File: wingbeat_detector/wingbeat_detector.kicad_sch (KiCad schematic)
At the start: 0 parts

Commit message: Rename to wingbeat_detector
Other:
- title: light_sensor_opt101 -> wingbeat_detector
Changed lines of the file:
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@@
   (paper "A4")
   (title_block
-    (title "light_sensor_opt101")
+    (title "wingbeat_detector")
     (date "2022-11-18")
     (rev "3.0.0")

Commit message: Add symbols and documentation
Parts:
- added P1: CONN_02X04_IC_DIP_RA_VERT, Janelia:HEADER_02x04, symbol Janelia:CONN_02X04_IC_DIP_RA_VERT
- added U1: UAF42, Janelia:SOIC_16, symbol Janelia:UAF42
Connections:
- no-connect marks 0 -> 2
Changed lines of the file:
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@@
   (title_block
     (title "wingbeat_detector")
-    (date "2022-11-18")
+    (date "2023-02-23")
     (rev "3.0.0")
     (company "Howard Hughes Medical Institute")
   )
+  (no_connect (at 96.52 81.28))
+  (no_connect (at 96.52 83.82))
+  (symbol (lib_id "Janelia:CONN_02X04_IC_DIP_RA_VERT") (at 90.17 82.55 0) (unit 1)
+    (in_bom yes) (on_board yes) (dnp no)
+    (property "Reference" "P1" (at 90.17 76.2 0)
+      (effects (font (size 1.27 1.27)))
+    )
+    (property "Value" "CONN_02X04_IC_DIP_RA_VERT" (at 90.17 88.9 0)
+      (effects (font (size 1.27 1.27)))
+    )
+    (property "Footprint" "Janelia:HEADER_02x04" (at 90.17 113.03 0)
+      (effects (font (size 1.524 1.524)) hide)
+    )
+    (property "Datasheet" "" (at 90.17 113.03 0)
+      (effects (font (size 1.524 1.524)))
+    )
+    (property "Vendor" "Digi-Key" (at 92.71 73.66 0)
+      (effects (font (size 1.524 1.524)) hide)
+    )
+    (property "Vendor Part Number" "A117-ND" (at 95.25 71.12 0)
+      (effects (font (size 1.524 1.524)) hide)
+    )
+    (property "Description" "CONN IC DIP SOCKET 8POS GOLD" (at 97.79 68.58 0)
+      (effects (font (size 1.524 1.524)) hide)
+    )
+    (property "Manufacturer" "Aries Electronics" (at 90.17 96.52 0)
+      (effects (font (size 1.27 1.27)) hide)
+    )
+    (property "Manufacturer Part Number" "08-810-90" (at 90.17 93.98 0)
+      (effects (font (size 1.27 1.27)) hide)
+    )
+    (pin "1")
+    (pin "2")
+    (pin "3")
+    (pin "4")
+    (pin "5")
+    (pin "6")
+    (pin "7")
+    (pin "8")
+    (instances
+      (project "wingbeat_detector"
+        (path "/cc457ebc-4af6-4663-b19f-8cb38f061cb4"
+          (reference "P1") (unit 1)
+        )
+      )
+    )
+  )
+  (symbol (lib_id "Janelia:UAF42") (at 162.56 83.82 0) (unit 1)
+    (in_bom yes) (on_board yes) (dnp no) (fields_autoplaced)
+    (property "Reference" "U1" (at 193.04 72.2883 0)
+      (effects (font (size 1.524 1.524)))
+    )
+    (property "Value" "UAF42" (at 193.04 74.8283 0)
+      (effects (font (size 1.524 1.524)))
+    )
+    (property "Footprint" "Janelia:SOIC_16" (at 184.15 72.39 0)
+      (effects (font (size 1.524 1.524)) hide)
+    )
+    (property "Datasheet" "" (at 186.69 69.85 0)
+      (effects (font (size 1.524 1.524)))
+    )
+    (property "Vendor" "Digi-Key" (at 189.23 67.31 0)
+      (effects (font (size 1.524 1.524)) hide)
+    )
+    (property "Vendor Part Number" "UAF42AU-ND" (at 191.77 64.77 0)
+      (effects (font (size 1.524 1.524)) hide)
+    )
+    (property "Description" "IC UNIV ACTIVE FILTER 16-SOIC" (at 194.31 62.23 0)
+      (effects (font (size 1.524 1.524)) hide)
+    )
+    (property "Manufacturer" "Texas Instruments" (at 162.56 83.82 0)
+      (effects (font (size 1.27 1.27)) hide)
+    )
+    (property "Manufacturer Part Number" "UAF42AU" (at 162.56 83.82 0)
+      (effects (font (size 1.27 1.27)) hide)
+    )
+    (pin "1")
+    (pin "10")
+    (pin "11")
+    (pin "12")
+    (pin "13")
+    (pin "14")
+    (pin "15")
+    (pin "16")
+    (pin "2")
+    (pin "3")
+    (pin "4")
+    (pin "5")
+    (pin "6")
+    (pin "7")
+    (pin "8")
+    (pin "9")
+    (instances
+      (project "wingbeat_detector"
+        (path "/cc457ebc-4af6-4663-b19f-8cb38f061cb4"
+          (reference "U1") (unit 1)
+        )
+      )
+    )
+  )
   (sheet_instances

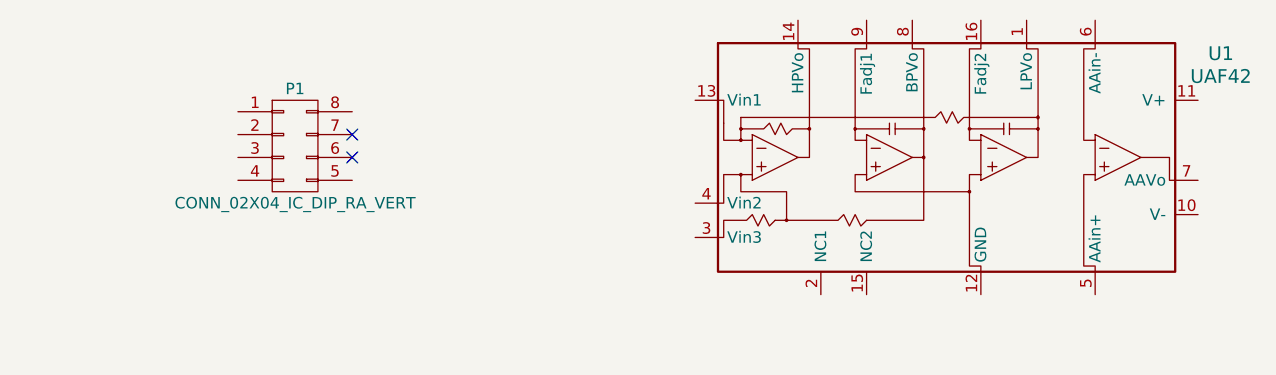
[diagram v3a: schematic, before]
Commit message: Add documentation and initial schematic part
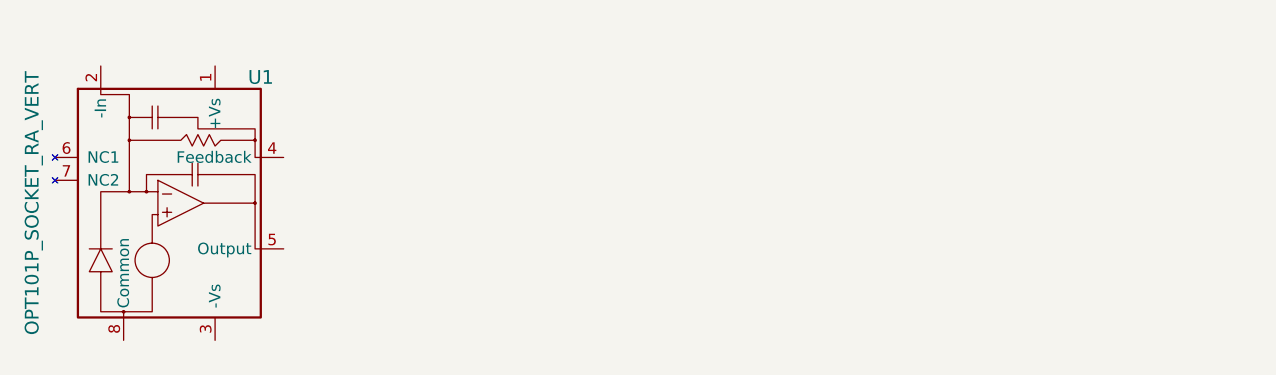
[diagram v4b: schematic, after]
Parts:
- removed P1: CONN_02X04_IC_DIP_RA_VERT, Janelia:HEADER_02x04, symbol Janelia:CONN_02X04_IC_DIP_RA_VERT
- removed U1: UAF42, Janelia:SOIC_16, symbol Janelia:UAF42
- added U1: OPT101P_SOCKET_RA_VERT, Janelia:SOCKET_DIP_02x04_RA_VERT, symbol Janelia:OPT101P_SOCKET_RA_VERT
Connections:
- no-connect marks 2 -> 0
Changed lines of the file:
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@@
     (company "Howard Hughes Medical Institute")
   )
-  (no_connect (at 96.52 81.28))
-  (no_connect (at 96.52 83.82))
-  (symbol (lib_id "Janelia:CONN_02X04_IC_DIP_RA_VERT") (at 90.17 82.55 0) (unit 1)
+  (symbol (lib_id "Janelia:OPT101P_SOCKET_RA_VERT") (at 76.2 88.9 0) (unit 1)
     (in_bom yes) (on_board yes) (dnp no)
-    (property "Reference" "P1" (at 90.17 76.2 0)
-      (effects (font (size 1.27 1.27)))
-    )
-    (property "Value" "CONN_02X04_IC_DIP_RA_VERT" (at 90.17 88.9 0)
-      (effects (font (size 1.27 1.27)))
-    )
-    (property "Footprint" "Janelia:HEADER_02x04" (at 90.17 113.03 0)
-      (effects (font (size 1.524 1.524)) hide)
-    )
-    (property "Datasheet" "" (at 90.17 113.03 0)
+    (property "Reference" "U1" (at 86.36 74.93 0)
       (effects (font (size 1.524 1.524)))
     )
-    (property "Vendor" "Digi-Key" (at 92.71 73.66 0)
-      (effects (font (size 1.524 1.524)) hide)
+    (property "Value" "OPT101P_SOCKET_RA_VERT" (at 60.96 88.9 90)
+      (effects (font (size 1.524 1.524)))
     )
-    (property "Vendor Part Number" "A117-ND" (at 95.25 71.12 0)
-      (effects (font (size 1.524 1.524)) hide)
-    )
-    (property "Description" "CONN IC DIP SOCKET 8POS GOLD" (at 97.79 68.58 0)
-      (effects (font (size 1.524 1.524)) hide)
-    )
-    (property "Manufacturer" "Aries Electronics" (at 90.17 96.52 0)
+    (property "Footprint" "Janelia:SOCKET_DIP_02x04_RA_VERT" (at 76.2 55.88 0)
       (effects (font (size 1.27 1.27)) hide)
     )
-    (property "Manufacturer Part Number" "08-810-90" (at 90.17 93.98 0)
+    (property "Datasheet" "" (at 76.2 88.9 0)
+      (effects (font (size 1.27 1.27)) hide)
+    )
+    (property "Manufacturer" "Aries Electronics" (at 76.2 58.42 0)
+      (effects (font (size 1.27 1.27)) hide)
+    )
+    (property "Manufacturer Part Number" "08-810-90" (at 76.2 63.5 0)
+      (effects (font (size 1.27 1.27)) hide)
+    )
+    (property "Vendor" "Digi-Key" (at 76.2 50.8 0)
+      (effects (font (size 1.27 1.27)) hide)
+    )
+    (property "Vendor Part Number" "A117-ND" (at 76.2 60.96 0)
+      (effects (font (size 1.27 1.27)) hide)
+    )
+    (property "Description" "CONN IC DIP SOCKET 8POS GOLD" (at 76.2 53.34 0)
       (effects (font (size 1.27 1.27)) hide)
     )
@@
     (instances
       (project "wingbeat_detector"
-        (path "/cc457ebc-4af6-4663-b19f-8cb38f061cb4"
-          (reference "P1") (unit 1)
-        )
-      )
-    )
-  )
-  (symbol (lib_id "Janelia:UAF42") (at 162.56 83.82 0) (unit 1)
-    (in_bom yes) (on_board yes) (dnp no) (fields_autoplaced)
-    (property "Reference" "U1" (at 193.04 72.2883 0)
-      (effects (font (size 1.524 1.524)))
-    )
-    (property "Value" "UAF42" (at 193.04 74.8283 0)
-      (effects (font (size 1.524 1.524)))
-    )
-    (property "Footprint" "Janelia:SOIC_16" (at 184.15 72.39 0)
-      (effects (font (size 1.524 1.524)) hide)
-    )
-    (property "Datasheet" "" (at 186.69 69.85 0)
-      (effects (font (size 1.524 1.524)))
-    )
-    (property "Vendor" "Digi-Key" (at 189.23 67.31 0)
-      (effects (font (size 1.524 1.524)) hide)
-    )
-    (property "Vendor Part Number" "UAF42AU-ND" (at 191.77 64.77 0)
-      (effects (font (size 1.524 1.524)) hide)
-    )
-    (property "Description" "IC UNIV ACTIVE FILTER 16-SOIC" (at 194.31 62.23 0)
-      (effects (font (size 1.524 1.524)) hide)
-    )
-    (property "Manufacturer" "Texas Instruments" (at 162.56 83.82 0)
-      (effects (font (size 1.27 1.27)) hide)
-    )
-    (property "Manufacturer Part Number" "UAF42AU" (at 162.56 83.82 0)
-      (effects (font (size 1.27 1.27)) hide)
-    )
-    (pin "1")
-    (pin "10")
-    (pin "11")
-    (pin "12")
-    (pin "13")
-    (pin "14")
-    (pin "15")
-    (pin "16")
-    (pin "2")
-    (pin "3")
-    (pin "4")
-    (pin "5")
-    (pin "6")
-    (pin "7")
-    (pin "8")
-    (pin "9")
-    (instances
-      (project "wingbeat_detector"
